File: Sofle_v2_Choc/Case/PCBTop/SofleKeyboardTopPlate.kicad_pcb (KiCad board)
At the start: 2 copper layers, 143.4 x 111.8 mm, 5 parts

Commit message: Text adjustments
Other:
- board text added: "Original Sofle design by Josef Adamacik"
- board text added: "https://josefadamcik.github.io/SofleKeyboard/"
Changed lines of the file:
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@@
   (general
     (thickness 1.6)
-    (drawings 160)
+    (drawings 164)
     (tracks 0)
     (zones 0)
@@
       (clearance 0.3))
   )
+  (gr_text "Original Sofle design by Josef Adamacik" (at 130.895 79.1 90) (layer F.Cu)
+    (effects (font (size 1 1) (thickness 0.2)))
+  )
+  (gr_text "Original Sofle design by Josef Adamacik" (at 130.995 79.3 270) (layer B.Cu)
+    (effects (font (size 1 1) (thickness 0.2)) (justify mirror))
+  )
+  (gr_text https://josefadamcik.github.io/SofleKeyboard/ (at 150.095 80.5 90) (layer F.Cu)
+    (effects (font (size 1 1) (thickness 0.15)))
+  )
+  (gr_text https://josefadamcik.github.io/SofleKeyboard/ (at 150.395 80.5 270) (layer B.Cu)
+    (effects (font (size 1 1) (thickness 0.15)) (justify mirror))
+  )
   (gr_line (start 112.995 38) (end 113.395 37.9) (layer Edge.Cuts) (width 0.15))

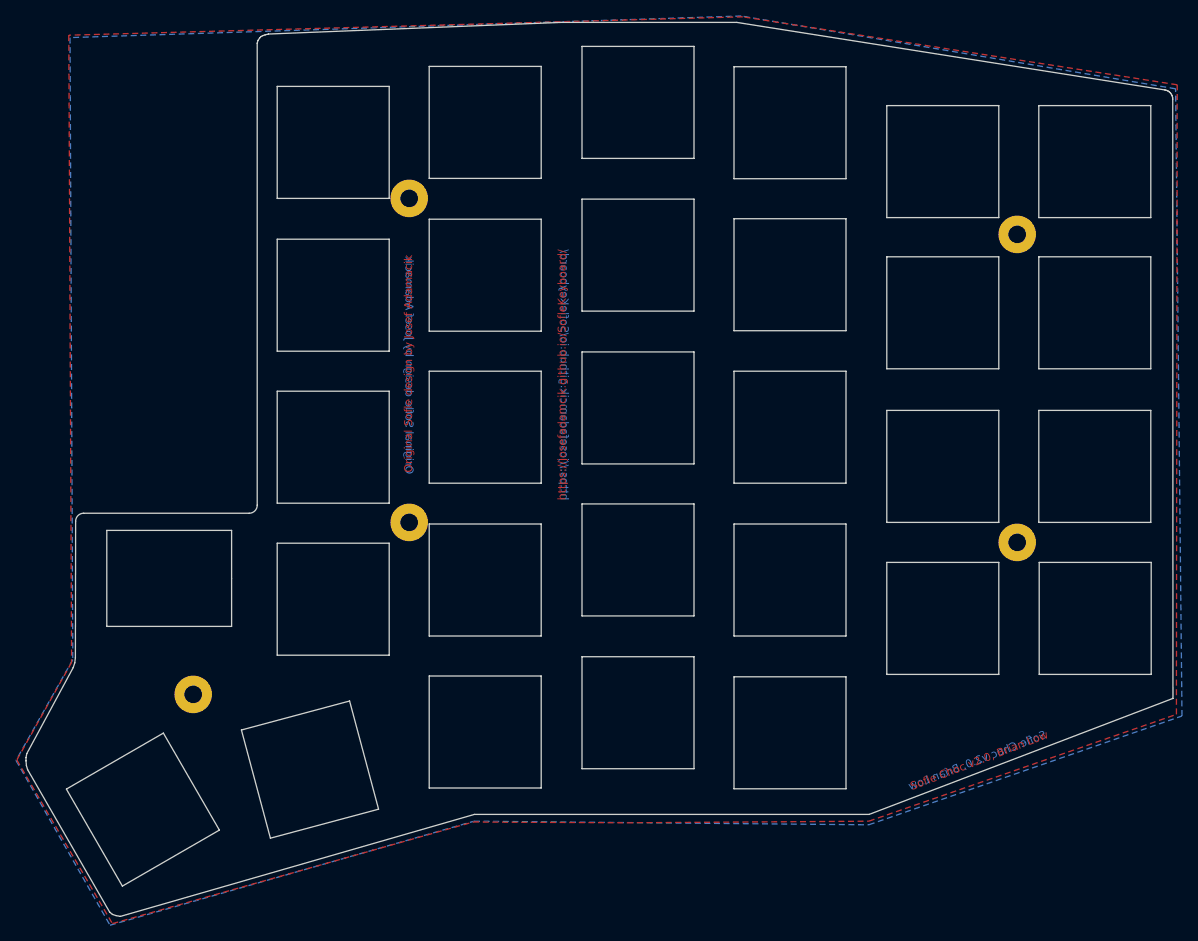
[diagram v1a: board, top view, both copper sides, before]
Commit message: Add footprints to top plate
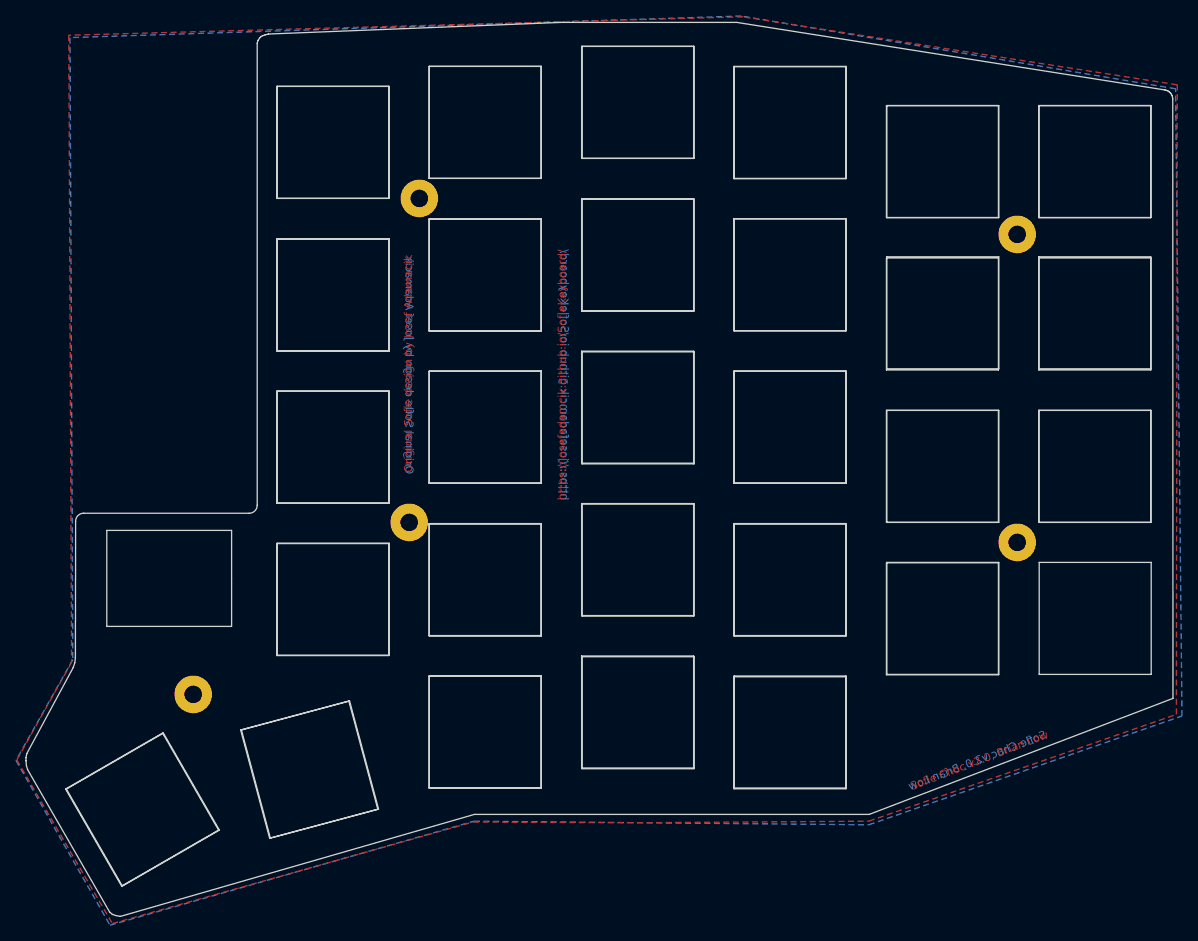
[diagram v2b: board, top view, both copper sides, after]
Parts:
- added SW2: KEY_SWITCH, SofleChocTop:SW_Hole, F.Cu at (97.6, 134.8)
- added SW2: KEY_SWITCH, SofleChocTop:SW_Hole, F.Cu at (140.5, 68.0)
- added SW2: KEY_SWITCH, SofleChocTop:SW_Hole, F.Cu at (140.5, 48.9)
- added SW2: KEY_SWITCH, SofleChocTop:SW_Hole, F.Cu at (159.5, 122.6)
- added SW2: KEY_SWITCH, SofleChocTop:SW_Hole, F.Cu at (159.5, 103.6)
- added SW2: KEY_SWITCH, SofleChocTop:SW_Hole, F.Cu at (159.5, 84.5)
- added SW2: KEY_SWITCH, SofleChocTop:SW_Hole, F.Cu at (159.5, 65.5)
- added SW2: KEY_SWITCH, SofleChocTop:SW_Hole, F.Cu at (159.5, 46.4)
- added SW2: KEY_SWITCH, SofleChocTop:SW_Hole, F.Cu at (178.6, 125.1)
- added SW2: KEY_SWITCH, SofleChocTop:SW_Hole, F.Cu at (178.6, 106.1)
- added SW2: KEY_SWITCH, SofleChocTop:SW_Hole, F.Cu at (178.6, 87.0)
- added SW2: KEY_SWITCH, SofleChocTop:SW_Hole, F.Cu at (118.5, 129.8)
- added SW2: KEY_SWITCH, SofleChocTop:SW_Hole, F.Cu at (178.6, 68.0)
- added SW2: KEY_SWITCH, SofleChocTop:SW_Hole, F.Cu at (178.6, 48.9)
- added SW2: KEY_SWITCH, SofleChocTop:SW_Hole, F.Cu at (197.6, 111.0)
- added SW2: KEY_SWITCH, SofleChocTop:SW_Hole, F.Cu at (216.7, 91.9)
- added SW2: KEY_SWITCH, SofleChocTop:SW_Hole, F.Cu at (197.6, 91.9)
- added SW2: KEY_SWITCH, SofleChocTop:SW_Hole, F.Cu at (216.7, 72.9)
- added SW2: KEY_SWITCH, SofleChocTop:SW_Hole, F.Cu at (197.6, 72.9)
- added SW2: KEY_SWITCH, SofleChocTop:SW_Hole, F.Cu at (197.6, 53.8)
- added SW2: KEY_SWITCH, SofleChocTop:SW_Hole, F.Cu at (216.7, 53.8)
- added SW2: KEY_SWITCH, SofleChocTop:SW_Hole, F.Cu at (121.4, 108.6)
- added SW2: KEY_SWITCH, SofleChocTop:SW_Hole, F.Cu at (121.4, 89.5)
- added SW2: KEY_SWITCH, SofleChocTop:SW_Hole, F.Cu at (121.4, 70.5)
- added SW2: KEY_SWITCH, SofleChocTop:SW_Hole, F.Cu at (121.4, 51.4)
- added SW2: KEY_SWITCH, SofleChocTop:SW_Hole, F.Cu at (140.5, 125.1)
- added SW2: KEY_SWITCH, SofleChocTop:SW_Hole, F.Cu at (140.5, 106.1)
- added SW2: KEY_SWITCH, SofleChocTop:SW_Hole, F.Cu at (140.5, 87.0)
- moved TH3 1.27 mm to (132.2, 58.5)

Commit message: Finalize layout - matches PCB now
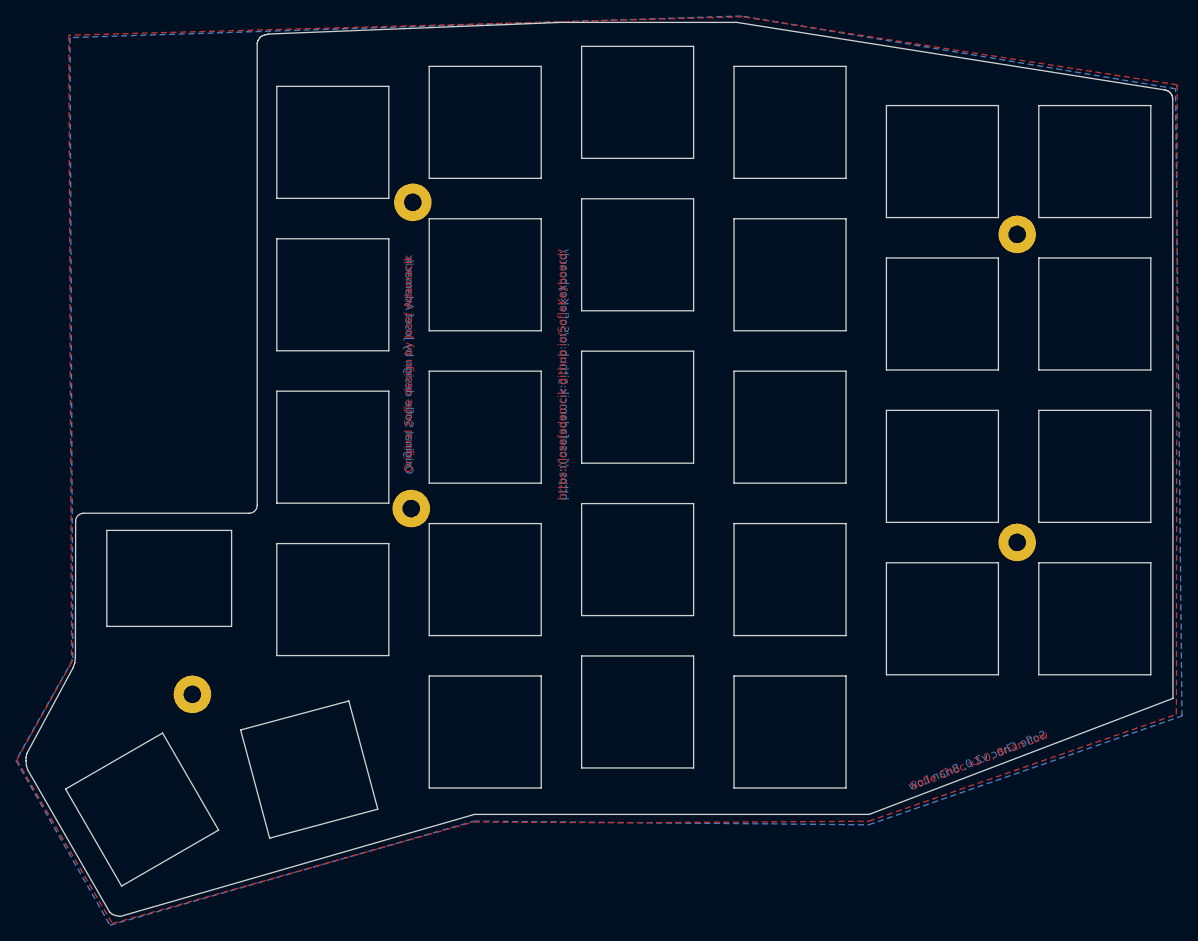
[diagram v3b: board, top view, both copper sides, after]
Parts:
- added SW2: KEY_SWITCH, SofleChocTop:SW_Hole, F.Cu at (216.7, 111.0)
- moved TH5 1.75 mm to (131.3, 97.3)
- moved TH3 0.95 mm to (131.4, 59.0)
- moved TH7 0.10 mm to (103.9, 120.4)
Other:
- outline, holes or cut-outs redrawn
